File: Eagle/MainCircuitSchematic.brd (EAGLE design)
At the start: 76.2 x 46.7 mm, 13 parts

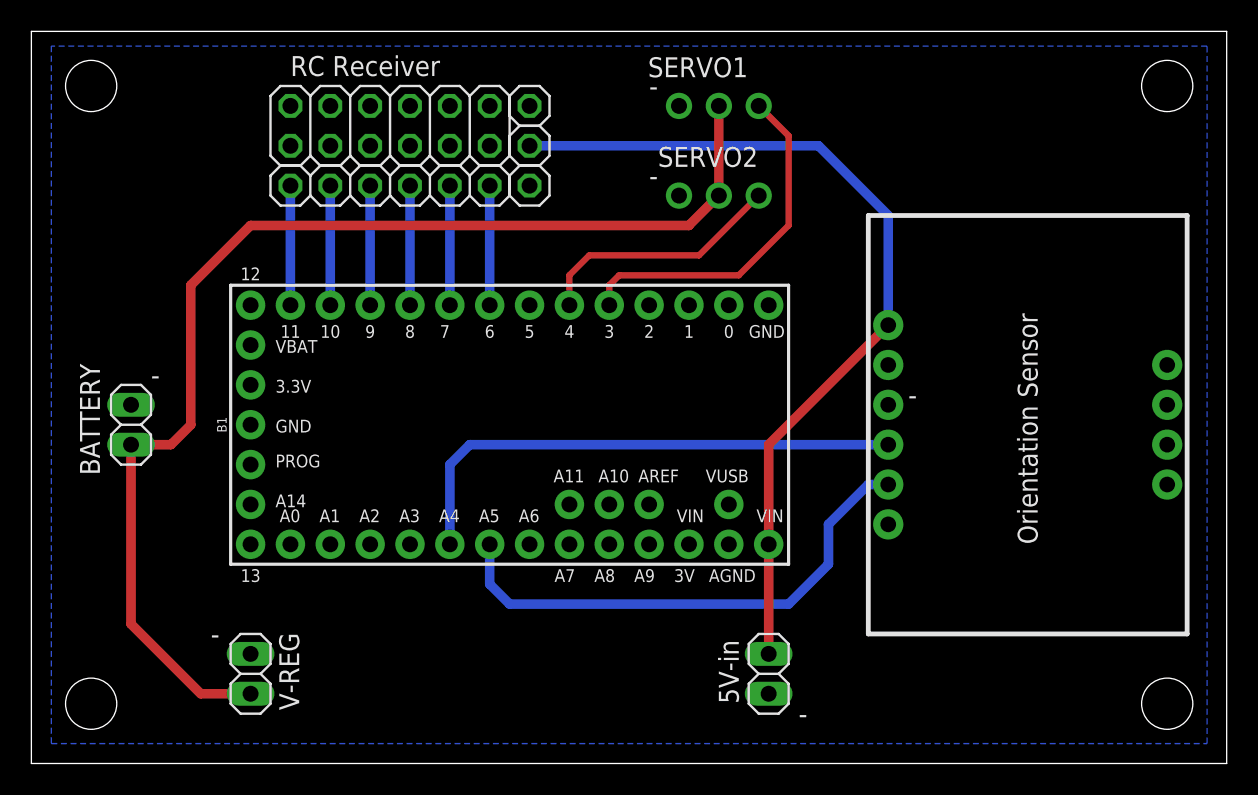
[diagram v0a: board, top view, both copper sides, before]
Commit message: added switch to design, removed excess receiver pins
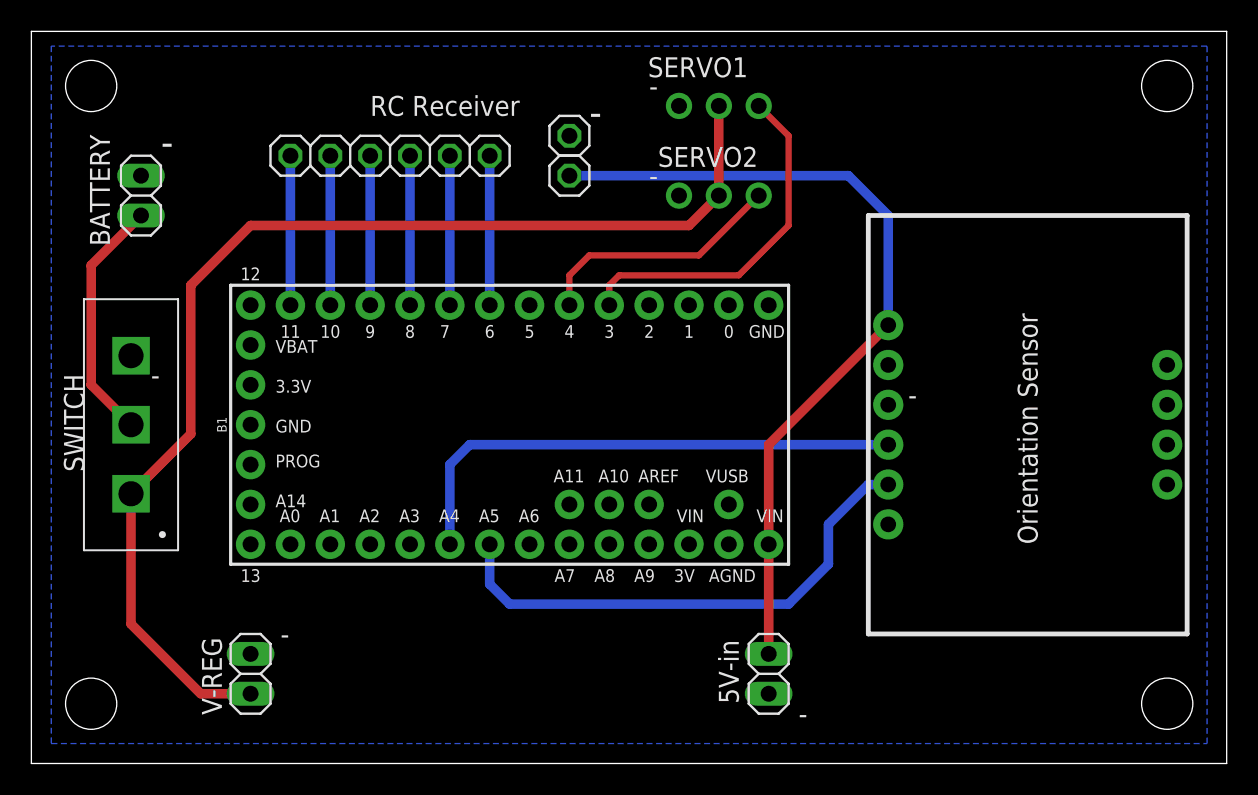
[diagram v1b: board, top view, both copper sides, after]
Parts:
- removed RECEIVNOTHING: (no value), pinhead:1X01
- removed UNUSEDRCRECEIVERCHANNELS: PINHD-2X6, Connector:2X06
- added SWITCH: 8SS1022-Z, ornithopter:8SS1022-Z
- moved BATTERY 14.6 mm to (73.0, 56.5)
- moved RECEIVPWR 3.17 mm to (100.3, 57.8)
- moved RECIEVGND 3.17 mm to (100.3, 60.3)
- moved RCRECEIVERCHANNELS 1.91 mm to (88.9, 59.1)
- turned V-REG to 90 degrees
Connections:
- removed net GND1: B1.GND1
- new net N$9: BATTERY.2, SWITCH.IN
- net 7.4V: now also SWITCH.OUT1, V-REG.1; no longer BATTERY.2, V-REG.2
- net GND: now also B1.GND1, V-REG.2; no longer V-REG.1
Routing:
- net N$9: track 0.00 -> 15.7 mm
- net 5V: track 55.8 -> 52.5 mm
- net 7.4V: track 77.1 -> 74.4 mm
- net N$6: track 7.62 -> 9.52 mm
- net N$5: track 7.62 -> 9.52 mm
- net N$4: track 7.62 -> 9.52 mm
- net N$3: track 7.62 -> 9.52 mm
- net N$2: track 7.62 -> 9.52 mm
- net N$1: track 7.62 -> 9.52 mm
